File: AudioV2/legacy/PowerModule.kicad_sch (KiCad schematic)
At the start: 14 parts, among them J201 +15/-15/A_GND out, J202 PD module in (1=GND 2=+12V), U201 REC10K-2415DAW/H2, U202 L7809CV +9V

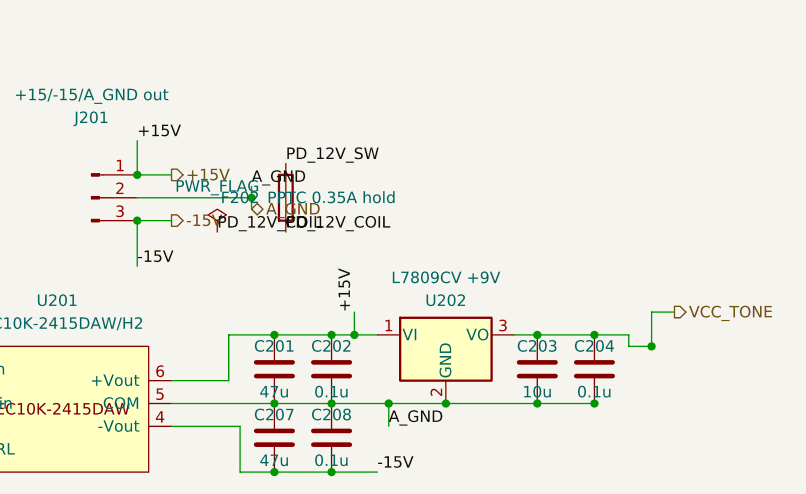
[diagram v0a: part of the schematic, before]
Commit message: AudioV2: D-f を実装した（+9V LDO 手前の PPTC 0.1A）。ゲート1は穴径だけ決めた
D-f —— 最後まで残っていた「各コンバータ手前に1本」の枝。

素材 legacy/PowerModule.kicad_sch を編集して再生成。+15V の T 点から U202.1 への
配線は 2.54 mm のスタブで 7.62 mm の素子が入らないため、D-g（F1603）と同じく
走行線から立ち上げて上で迂回し、F203 を縦置きにした。下流が無名ネットになり
power_pin_not_driven が出るので PWR_FLAG を1つ足してある。

  +15V(144.78,77.47) up (144.78,66.04) -> (147.32,66.04) down F203 down U202.VI(147.32,77.47)

⚠ これは保護の欠落を埋めたのではなく、方針の対称性。否定側査読の指摘どおり技術的
必須ではない（上流に主系ヒューズ、枝は ~30 mA、L7809 の熱保護もある）。残す判断の
理由は「1枝だけ幾何の都合で例外」を文書に抱え続けるコストの方が高いこと。定格
0.1 A はゲート3（U1604 の負荷電流実測）で再判定する。直列抵抗の落ちは 30 mA で
0.06〜0.15 V、±12 V 化時のヘッドルーム 3.0 V に対し 2〜5%。

ゲート1 —— 決めたのは穴径であって型番ではない。PCB は REC20K の穴径・ピン配置で
起こす。Ø1.0 → Ø1.4 の穴で起こせば REC10K は後からドロップインで戻せる（逆は不可）。
型番はゲート3とセットで決める: REC20K の代償である絶縁容量 1000 → 2000 pF の不利は
U1604 による既存のグランド結合への上乗せなので、U1604 を三端子へ替えるかで大きさが
変わるため。回路図の Value は REC10K-2415DAW/H2 のまま。

⚠ 1.2 kHz スパーでは絶縁容量の是非を判定できない（1000pF=133kΩ / 2000pF=66kΩ）。
効くのはスイッチング帯以上で、出方は ADC の床の持ち上がり。測る道具が別。

腐っていたドキュメントを4件直した:
  PARTS.md                     「PPTC は回路図には未追加」（3本すでにあった）
  AGENT_HANDOFF                「D-f/D-g PPTC 未実装2件」（D-g は 2026-09-04 に実装済み）
  DECISIONS 実装表 / +9V 共有表   D-f の「未実装」

検証（Windows / Git Bash / KiCad 10.0.6 / Docker 無し）:
  erc            29 件（内訳も従前と完全一致）
  netlist        部品 374 / 重複 0 / 注釈警告なし（373->374 は F203。PWR_FLAG は仮想で計上外）
  +15V           F203.1 を含み U202.1 は外れた
  新ネット        Net-(U202-VI) = [F203.2, U202.1]
  roundtrip      10 ファイル OK
  check_sexpr    問題 0
  再生成の冪等性   2回回して追加差分なし

Co-Authored-By: Claude Opus 5 <noreply@anthropic.com>
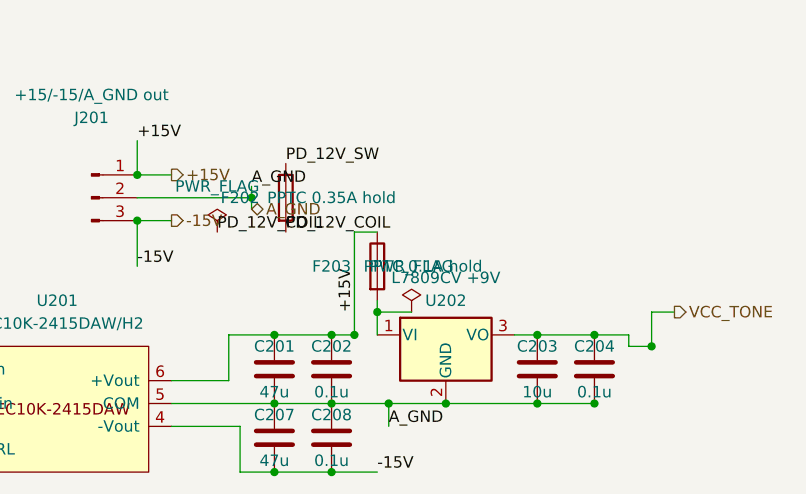
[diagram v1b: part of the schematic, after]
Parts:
- added F203: PPTC 0.1A hold, symbol Device:Fuse
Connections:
- net +15V: now also F203.1; no longer U202.1 (VI)
- new net: F203.2, U202.1 (VI)
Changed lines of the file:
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@@
-	(wire
-		(pts
-			(xy 144.78 77.47) (xy 147.32 77.47)
-		)
-		(stroke
-			(width 0)
-			(type default)
-		)
-	)
 	(wire
 		(pts
@@
 	(wire
 		(pts
-			(xy 144.78 74.93) (xy 144.78 77.47)
+			(xy 144.78 66.04) (xy 144.78 77.47)
 		)
 		(stroke
@@
 		)
 	)
+	(wire
+		(pts
+			(xy 144.78 66.04) (xy 147.32 66.04)
+		)
+		(stroke
+			(width 0)
+			(type default)
+		)
+	)
+	(wire
+		(pts
+			(xy 147.32 73.66) (xy 147.32 74.93)
+		)
+		(stroke
+			(width 0)
+			(type default)
+		)
+	)
+	(wire
+		(pts
+			(xy 147.32 74.93) (xy 147.32 77.47)
+		)
+		(stroke
+			(width 0)
+			(type default)
+		)
+	)
+	(wire
+		(pts
+			(xy 147.32 74.93) (xy 151.13 74.93)
+		)
+		(stroke
+			(width 0)
+			(type default)
+		)
+	)
+	(junction
+		(at 147.32 74.93)
+		(diameter 0)
+		(color 0 0 0 0)
+	)
+	(symbol
+		(lib_id "Device:Fuse")
+		(at 147.32 69.85 0)
+		(unit 1)
+		(body_style 1)
+		(exclude_from_sim no)
+		(in_bom yes)
+		(on_board yes)
+		(in_pos_files yes)
+		(dnp no)
+		(property "Reference" "F203"
+			(at 142.24 69.85 0)
+			(show_name no)
+			(do_not_autoplace no)
+			(effects
+				(font
+					(size 1.27 1.27)
+				)
+			)
+		)
+		(property "Value" "PPTC 0.1A hold"
+			(at 152.4 69.85 0)
+			(show_name no)
+			(do_not_autoplace no)
+			(effects
+				(font
+					(size 1.27 1.27)
+				)
+			)
+		)
+		(property "Footprint" ""
+			(at -12.7 45.72 0)
+			(hide yes)
+			(show_name no)
+			(do_not_autoplace no)
+			(effects
+				(font
+					(size 1.27 1.27)
+				)
+			)
+		)
+		(property "Datasheet" ""
+			(at -12.7 45.72 0)
+			(hide yes)
+			(show_name no)
+			(do_not_autoplace no)
+			(effects
+				(font
+					(size 1.27 1.27)
+				)
+			)
+		)
+		(property "Description" ""
+			(at -12.7 45.72 0)
+			(hide yes)
+			(show_name no)
+			(do_not_autoplace no)
+			(effects
+				(font
+					(size 1.27 1.27)
+				)
+			)
+		)
+		(pin "1"
+		)
+		(pin "2"
+		)
+		(instances
+			(project "AudioV2Case"
+				(path "/a1000001-0001-4001-8001-000000000001/a1000002-0002-4002-8002-000000000002"
+					(reference "F203")
+					(unit 1)
+				)
+			)
+		)
+	)
 	(label "PD_12V_SW"
 		(at 137.16 58.42 0)
@@
 					(unit 1)
 				)
+			)
+		)
+	)
+	(symbol
+		(lib_id "power:PWR_FLAG")
+		(at 151.13 74.93 0)
+		(unit 1)
+		(body_style 1)
+		(exclude_from_sim no)
+		(in_bom yes)
+		(on_board yes)
+		(in_pos_files yes)
+		(dnp no)
+		(fields_autoplaced yes)
+		(property "Reference" "#FLG0204"
+			(at 151.13 72.39 0)
+			(hide yes)
+			(show_name no)
+			(do_not_autoplace no)
+			(effects
+				(font
+					(size 1.27 1.27)
+				)
+			)
+		)
+		(property "Value" "PWR_FLAG"
+			(at 151.13 69.85 0)
+			(show_name no)
+			(do_not_autoplace no)
+			(effects
+				(font
+					(size 1.27 1.27)
+				)
+			)
+		)
+		(property "Footprint" ""
+			(at 74.93 88.9 0)
+			(hide yes)
+			(show_name no)
+			(do_not_autoplace no)
+			(effects
+				(font
+					(size 1.27 1.27)
+				)
+			)
+		)
+		(property "Datasheet" ""
+			(at 74.93 88.9 0)
+			(hide yes)
+			(show_name no)
+			(do_not_autoplace no)
+			(effects
+				(font
+					(size 1.27 1.27)
+				)
+			)
+		)
+		(property "Description" "Special symbol for telling ERC where power comes from"
+			(at 74.93 88.9 0)
+			(hide yes)
+			(show_name no)
+			(do_not_autoplace no)
+			(effects
+				(font
+					(size 1.27 1.27)
+				)
+			)
+		)
+		(pin "1"
+		)
+		(instances
+			(project "AudioV2Case"
+				(path "/a1000001-0001-4001-8001-000000000001/a1000002-0002-4002-8002-000000000002"
+					(reference "#FLG0204")
+					(unit 1)
+				)

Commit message: AudioV2: 母板のフットプリント 23 個を設計内の前例に合わせて埋めた（39 -> 16）
B5 の下ごしらえ。前例のあるものだけを埋め、判断が要るものには触っていない。

  積セラ 1206     C202/204/206/208/402, C403/404/410/411, C408/412
                  設計で 85 回使われている流儀に合わせた
  抵抗 1206       R410/411（同 128 回）
  フィルム        C405/406/407/409（2.2u）
                  PT2314 の入出力結合で音声が通る。設計内の C601「2.2uF film」と
                  同じ footprint に揃えた。セラミックは電圧で容量が変わるので
                  結合位置に置くと歪む（ユーザー判断 2026-09-07）
  電解            C201/205/207(47u) -> D8.0/P3.50（C1610・C1621 と同じ）
                  C401(22u)         -> D6.3/P2.50（C1630 と同じ）
                  C203(10u)         -> D5.0/P2.00（C1635「10uF 50V」と同じ）
  DC-DC           U403 -> Library:BP5293-50_ROHM_SIP-3
                  U1607 が同一部品で同じ footprint

素材（legacy/ControlPanelAnalog 15個・legacy/PowerModule 8個）を編集して再生成した。

**残り 16 個には触っていない。** 性質が2つに分かれる:

  パネル部品 6（RV501/502・SW501/502/1601・SW402）
    KiCad にもプロジェクトの Audio/Library.pretty にも footprint が無い。
    Alps は RK097/RK09K しかなく RK27 は別物。C&K 7000 系トグルも無い。
    データシートから新規に作る作業になる。
    さらに SW501/502/1601 は現物1個の 3PDT を3シンボルで表しているので、
    3つ全部に footprint を入れると PCB にスイッチが3個並ぶ。1個化が要る。

  調達判断待ち 10（D403・F201/202/203・J201/202・J_HP501・J_LINE501・
    J_RAIL501・U202）

検証:
  未設定      39 -> 16
  netlist     部品 370 / 重複 0（変化なし）
  erc         17 件（変化なし）
  check_sexpr 13 ファイル / 問題 0
  roundtrip   6/6 OK
  再生成      2回目でバイト一致

Co-Authored-By: Claude Opus 5 <noreply@anthropic.com>
Claude-Session: https://claude.ai/code/session_01VCArLcCGbMGgxvWJ5HFJiY
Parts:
- C201, C205, C207: footprint (none) -> Capacitor_THT:CP_Radial_D8.0mm_P3.50mm
- C202, C204, C206, C208: footprint (none) -> Capacitor_SMD:C_1206_3216Metric_Pad1.33x1.80mm_HandSolder
- C203: footprint (none) -> Capacitor_THT:CP_Radial_D5.0mm_P2.00mm
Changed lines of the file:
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@@
 			)
 		)
-		(property "Footprint" ""
+		(property "Footprint" "Capacitor_THT:CP_Radial_D5.0mm_P2.00mm"
 			(at 22.86 10.16 0)
 			(hide yes)
@@
 			)
 		)
-		(property "Footprint" ""
+		(property "Footprint" "Capacitor_THT:CP_Radial_D8.0mm_P3.50mm"
 			(at -1.27 20.32 0)
 			(hide yes)
@@
 			)
 		)
-		(property "Footprint" ""
+		(property "Footprint" "Capacitor_SMD:C_1206_3216Metric_Pad1.33x1.80mm_HandSolder"
 			(at -62.23 21.59 0)
 			(hide yes)
@@
 			)
 		)
-		(property "Footprint" ""
+		(property "Footprint" "Capacitor_SMD:C_1206_3216Metric_Pad1.33x1.80mm_HandSolder"
 			(at 3.81 10.16 0)
 			(hide yes)
@@
 			)
 		)
-		(property "Footprint" ""
+		(property "Footprint" "Capacitor_SMD:C_1206_3216Metric_Pad1.33x1.80mm_HandSolder"
 			(at -7.62 17.78 0)
 			(hide yes)
@@
 			)
 		)
-		(property "Footprint" ""
+		(property "Footprint" "Capacitor_SMD:C_1206_3216Metric_Pad1.33x1.80mm_HandSolder"
 			(at -7.62 25.4 0)
 			(hide yes)
@@
 			)
 		)
-		(property "Footprint" ""
+		(property "Footprint" "Capacitor_THT:CP_Radial_D8.0mm_P3.50mm"
 			(at -1.27 17.78 0)
 			(hide yes)
@@
 			)
 		)
-		(property "Footprint" ""
+		(property "Footprint" "Capacitor_THT:CP_Radial_D8.0mm_P3.50mm"
 			(at -8.89 31.75 0)
 			(hide yes)

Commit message: AudioV2: 端子台5個を Phoenix MKDS-1,5 にした（10 -> 5）
ユーザー判断（2026-09-07）。PARTS.md:211 が板間の端子台に Phoenix MKDS-1,5
系を指定しており、計測基板の J1601(2P) / J1603(3P) に既に同じ footprint が
入っている。その前例に合わせた。

  J201       1x03  +15/-15/A_GND out
  J202       1x02  PD module in
  J_HP501    1x02  to Audio HP Buffer
  J_LINE501  1x02  LINE OUT
  J_RAIL501  1x03  RAIL IN

J_HP501 / J_LINE501 / J_RAIL501 は元から Connector:Screw_Terminal_01xNN
シンボルなので端子台が自然。J201 / J202 は Conn_01xNN_Pin（汎用ピン）だが、
板間の電源なので同じ系に揃えた。

残り5個は性質が違うので手を付けていない:
  D403             12V パネル LED。直列抵抗の有無が未決（DECISIONS の既知項目）
  F201             T1.6A slow 5x20。ヒューズホルダの品種
  F202/F203        PPTC。MPN 未確定（直流抵抗とディレーティングが決まらない）
  U202             L7809CV TO-220。実装向き（垂直/水平・放熱器）が機構判断

検証:
  未設定      10 -> 5
  netlist     部品 370 / 重複 0（変化なし）
  erc         17 件（変化なし）
  check_sexpr 13 ファイル / 問題 0
  roundtrip   6/6 OK
  再生成      2回目でバイト一致

Co-Authored-By: Claude Opus 5 <noreply@anthropic.com>
Claude-Session: https://claude.ai/code/session_01VCArLcCGbMGgxvWJ5HFJiY
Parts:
- J201: footprint (none) -> TerminalBlock_Phoenix:TerminalBlock_Phoenix_MKDS-1,5-3-5.08_1x03_P5.08mm_Horizontal
- J202: footprint (none) -> TerminalBlock_Phoenix:TerminalBlock_Phoenix_MKDS-1,5-2-5.08_1x02_P5.08mm_Horizontal
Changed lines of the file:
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@@
 			)
 		)
-		(property "Footprint" ""
+		(property "Footprint" "TerminalBlock_Phoenix:TerminalBlock_Phoenix_MKDS-1,5-2-5.08_1x02_P5.08mm_Horizontal"
 			(at 26.67 -5.08 0)
 			(hide yes)
@@
 			)
 		)
-		(property "Footprint" ""
+		(property "Footprint" "TerminalBlock_Phoenix:TerminalBlock_Phoenix_MKDS-1,5-3-5.08_1x03_P5.08mm_Horizontal"
 			(at -59.69 6.35 0)
 			(hide yes)

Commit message: AudioV2: 残り5個のフットプリントを埋めた（5 -> 0）。D403 に直列抵抗 R401
フットプリント未設定 0 個。これで netlist 上の 371 部品すべてに footprint が付いた。

- F201/F202/F203 … Resistor_THT:R_Axial_DIN0411_L9.9mm_D3.6mm_P12.70mm_Horizontal
  設計内の F1601/F1602/F1603 と同じリード品に揃えた。ピッチが3種類に散らばる
  より、入手性のいい 5x20mm 相当の軸形1種に寄せたほうが調達が楽になる
- U202 … Package_TO_SOT_THT:TO-220-3_Vertical
  垂直立て。放熱器の要否と向きは PCB を起こすとき（B5）に決め直す
- D403 … LED_THT:LED_D5.0mm（設計内の D1610/D1611 と同じ）

D403 は PD_12V_SW に直付けだったので、電流制限の 2.2k を直列に入れた:

    PD_12V_SW ─[R401 2.2k]─ LED_12V_A ─[D403]─ PD_GND

抵抗なしだと LED の Vf ばらつきがそのまま電流に出る。12V で Vf 2.0V 想定なら
約 4.5mA。部品数 370 -> 371（CLAUDE.md の期待値も更新）。

生成シートは直接触らず、素材の legacy/ControlPanelAnalog.kicad_sch と
legacy/PowerModule.kicad_sch を編集して build_daughter -> build_motherboard で
再生成した。

検証:
  check_sexpr.py -q AudioV2        13 ファイル / 問題 0
  kicad-run.sh erc                 17 件（変化なし）
  kicad-run.sh netlist             部品 371 個・重複 0・footprint 未設定 0
  sch_import.py --roundtrip        6/6 OK
  再生成の冪等性                    バイト一致

⚠ PARTS.md の「音声 2×4」は「4ピンのヘッダを2組」と読んで 2 x PinHeader_1x04 に
した。2行4列（PinHeader_2x04）のつもりだったなら直す必要がある。

Co-Authored-By: Claude Opus 5 <noreply@anthropic.com>
Claude-Session: https://claude.ai/code/session_01VCArLcCGbMGgxvWJ5HFJiY
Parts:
- F201, F202, F203: footprint (none) -> Resistor_THT:R_Axial_DIN0411_L9.9mm_D3.6mm_P12.70mm_Horizontal
- U202: footprint (none) -> Package_TO_SOT_THT:TO-220-3_Vertical
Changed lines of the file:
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@@
 			)
 		)
-		(property "Footprint" ""
+		(property "Footprint" "Package_TO_SOT_THT:TO-220-3_Vertical"
 			(at 0 11.43 0)
 			(hide yes)
@@
 			)
 		)
-		(property "Footprint" ""
+		(property "Footprint" "Resistor_THT:R_Axial_DIN0411_L9.9mm_D3.6mm_P12.70mm_Horizontal"
 			(at -12.7 45.72 0)
 			(hide yes)
@@
 			)
 		)
-		(property "Footprint" ""
+		(property "Footprint" "Resistor_THT:R_Axial_DIN0411_L9.9mm_D3.6mm_P12.70mm_Horizontal"
 			(at -12.7 45.72 0)
 			(hide yes)
@@
 			)
 		)
-		(property "Footprint" ""
+		(property "Footprint" "Resistor_THT:R_Axial_DIN0411_L9.9mm_D3.6mm_P12.70mm_Horizontal"
 			(at -12.7 45.72 0)
 			(hide yes)

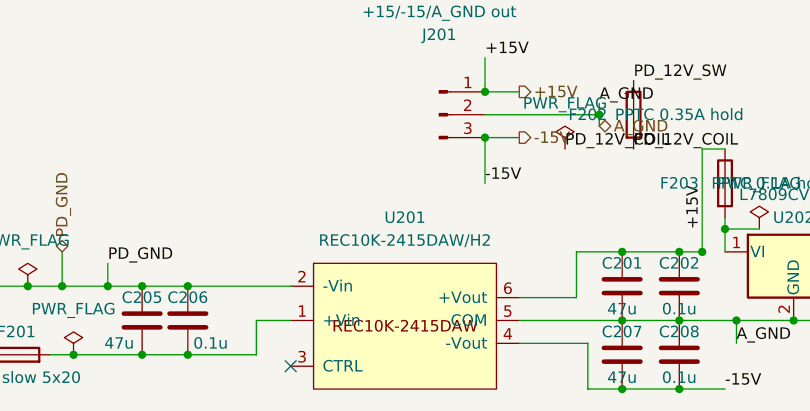
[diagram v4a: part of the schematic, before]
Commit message: AudioV2: DC-DC を REC20K-2415DZ へ差し替え、電源要求を「ソケットあたり」で記録した
## なぜ

この箱はオペアンプを差し替えて聴く箱で、入力ブロードキャスト＋出力のみ MUX なので
10個が常時通電する。つまり +15V の要求は「NE5532 ×10」ではなく「挿す石 ×10、常時」で、
レールの余裕は**1ソケットあたり何 mA 使えるか**に翻訳しないと目的と噛み合わない。

Audio/datasheets/opamps/ の一次資料（在庫石の Icc）:
  MUSES03  20 mA/socket（10 mA max ×2 の変換基板）← 在庫の最悪
  NE5532   16 mA（ICC total、VO=0 無負荷。typ 6 mA）
  OPA627×2 15 mA / LT1364 15 mA / OPA1656 9.2 mA/pkg max

1ソケットあたりに使える電流（固定側を保守側の 63 mA として）:

              計測系そのまま  LDO を +15V へ  +5V_D も +15V へ
  REC10K       27.0 mA        19.0 mA         9.4 mA
  REC20K       60.4 mA        52.4 mA        42.8 mA

REC10K では計測系を触らなくても 27 mA/socket しか出ない。MUSES03(20mA) は通るが
ディスクリート DIP-8 モジュールは入らず、計測系を +15V へ寄せると NE5532 の max
16 mA すら割る。「差し替えて遊ぶ」という目的に対して REC10K は最初から窮屈だった。

## 差し替え

独立した3つの理由が同じ結論に集まった:
  ① 上のソケットあたり予算
  ② Cout の宿題 — 実レール容量は +15V/-15V とも 259.8uF（sch_facts rails）で
     REC10K の Cout ±270uF の 96%。記録が使ってきた「102uF」は娘基板のバルクが
     入る前の古い値だった。REC20K は ±3000uF で 11 倍の余裕
  ③ 計測系の電源を +15V へ寄せる余地（U1604 = 非絶縁バック = 1.2kHz スパーの
     容疑者を設計から消せる。これ自体は未実施）

DS を突き合わせた結果（Recom_REC20K-Z_Rev3-2025.pdf p9 / REC10K-AW_Rev2-2025.pdf p9）:
入力 9-36V・ピン配置・パッド座標は同一で、**違うのは推奨穴だけ**（Ø1.0 -> Ø1.4）。

  ⚠ NOW.md は以前から「PCB の穴径は REC20K 互換（Ø1.4）」と書いていたが、
    フットプリント REC10K-AW_1in_THT は drill 1.0 のままで意図が実装されていなかった。
    REC20K の 1.4mm ピンは入らない。

Library:REC20K-Z_1in_THT を新設（穴 Ø1.4・パッド 2.2mm で環状部 0.4mm 維持）。
Ø1.4 なら REC10K（ピン径 0.6）も挿さるので、この1個で両方いける
= NOW.md の「REC10K は後から戻せる」が本当に成立する形になった。

  AudioV2.kicad_sym            REC20K-2415DZ を追加（REC10K とピン配置同一）
  legacy/PowerModule.kicad_sch U201 の lib_id/Value/Footprint/Datasheet/Description
                               ⚠ .kicad_sch は先頭に lib_symbols のキャッシュを持つので
                                 キャッシュと実体の2箇所を直す必要がある

## F201（入口 T1.6A）は据え置いたが、意味が変わった

12V 入力・効率 88% で:
  いまの想定（10×20mA + 固定 63mA）  7.9 W → 0.75 A  (T1.6A の 47%)
  計測系を +15V へ寄せたとき        10.5 W → 1.00 A  (62%)
  REC20K を使い切ったとき           20.0 W → 1.89 A  (118%)

つまり F201 が「REC20K の能力ではなく設計予算」を上限にしている。意図的なら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
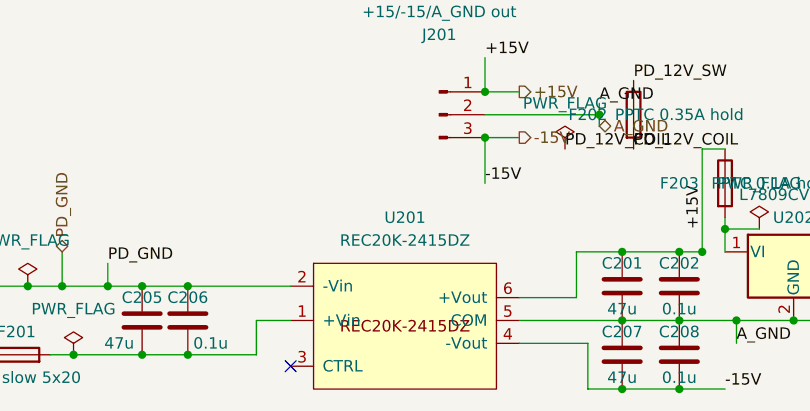
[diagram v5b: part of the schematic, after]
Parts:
- U201: value REC10K-2415DAW/H2 -> REC20K-2415DZ; footprint Library:REC10K-AW_1in_THT -> Library:REC20K-Z_1in_THT; symbol AudioV2:REC10K-2415DAW -> AudioV2:REC20K-2415DZ; MPN REC10K-2415DAW/H2 -> REC20K-2415DZ
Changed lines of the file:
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@@
 	)
 	(symbol
-		(lib_id "AudioV2:REC10K-2415DAW")
+		(lib_id "AudioV2:REC20K-2415DZ")
 		(at 111.76 76.2 0)
 		(unit 1)
@@
 			)
 		)
-		(property "Value" "REC10K-2415DAW/H2"
+		(property "Value" "REC20K-2415DZ"
 			(at 111.76 76.2 0)
 			(show_name no)
@@
 			)
 		)
-		(property "Footprint" "Library:REC10K-AW_1in_THT"
+		(property "Footprint" "Library:REC20K-Z_1in_THT"
 			(at 113.03 72.39 0)
 			(hide yes)
@@
 			)
 		)
-		(property "Datasheet" "https://recom-power.com/pdf/Econoline/REC10K-AW.pdf"
+		(property "Datasheet" "AudioV2/datasheets/Recom_REC20K-Z_Rev3-2025.pdf"
 			(at 112.268 74.422 0)
 			(hide yes)
@@
 			)
 		)
-		(property "Description" "Recom REC10K-2415DAW/H2 isolated DC/DC, 9-36Vin, ±15V/±333mA (10W), 1.6kVDC iso, DIP 1in x 1in, Cout ±270uF/rail, pin3=CTRL open=ON"
+		(property "Description" "Recom REC20K-2415DZ isolated DC/DC, 9-36Vin, ±15V/±667mA (20W), eff 88% typ, DIP 1in x 1in, Cout ±3000uF/rail, pin3=CTRL open=ON。REC10K-2415DAW/H2（±333mA・Cout ±270uF）から 2026-09-07 に差し替えた。理由は独立に3つ: ①ソケット10個が常時通電なので ±333mA だと 1ソケットあたり 27mA しか使えず、在庫の MUSES03（20mA）で既に窮屈 ②実レール容量 259.8uF が Cout ±270uF の 96% ③計測系の電源を +15V へ寄せる余地。ピン配置は REC10K と同一で、推奨穴が Ø1.0 -> Ø1.4 になるのでフットプリントも替えた（Ø1.4 なら REC10K も挿さる）"
 			(at 111.76 76.2 0)
 			(hide yes)
@@
 			)
 		)
-		(property "MPN" "REC10K-2415DAW/H2"
+		(property "MPN" "REC20K-2415DZ"
 			(at 111.76 76.2 0)
 			(hide yes)

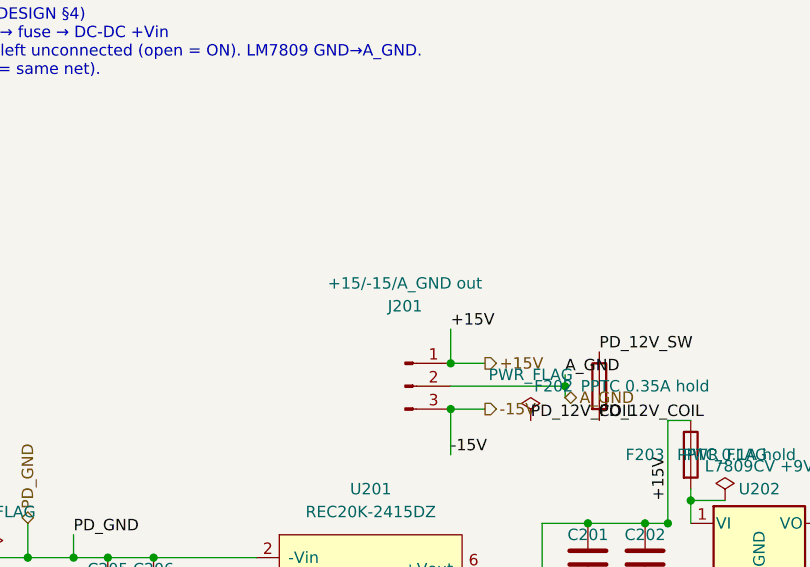
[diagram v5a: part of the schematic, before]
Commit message: AudioV2: J1602 / J1603 のピン並びを母板の J202 / J201 に揃えた
計測側の電源端子が母板側と逆順だった（J1603: -15/GND/+15 vs J201: +15/A_GND/-15、
J1602: +12V/GND vs J202: GND/+12V）。配線・ラベル・F1601 は動かさず、シンボルを
左右ミラーしてピンの x を入れ替えた（J1602 はアンカーも 1 ピッチ移動）。
J201 の Value「+15/-15/A_GND out」を実ピン順「+15/A_GND/-15 out」に直した（素材 → 再生成）。
端子を残すか外すかは B5 のハーネス判断のまま。J1601（AUDIO、R/L 2P）は J_RAIL501（L/A_GND/R 3P）
と形が違う点を NOW に書いた。

検証: kicad-cli ネットリストで J1603 1=+15V 2=A_GND 3=-15V、J1602 1=PD_GND 2=F1601 側を確認。
ERC 11 件（変化なし）・部品 389・重複 0・check_sexpr 0・roundtrip OK・再生成バイト一致。

Co-Authored-By: Claude Fable 5.1 <noreply@anthropic.com>
Claude-Session: https://claude.ai/code/session_01VCArLcCGbMGgxvWJ5HFJiY
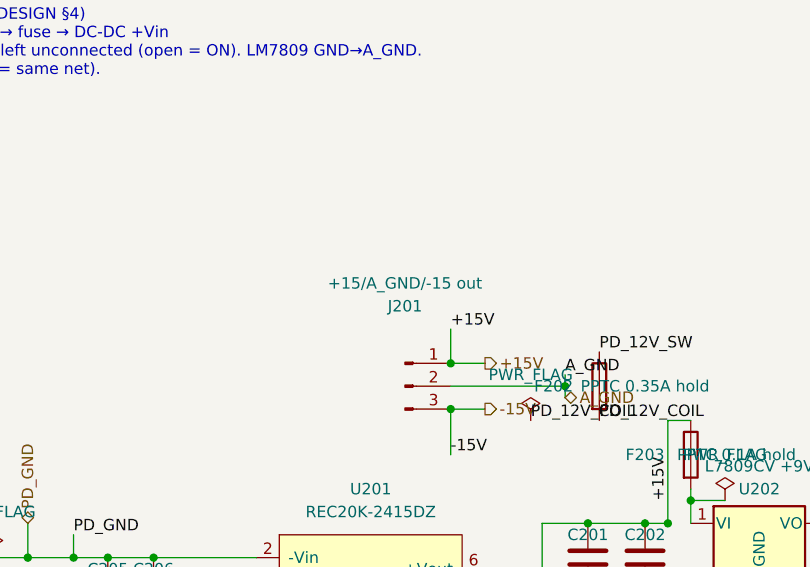
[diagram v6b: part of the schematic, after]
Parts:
- J201: value +15/-15/A_GND out -> +15/A_GND/-15 out
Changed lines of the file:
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@@
 			)
 		)
-		(property "Value" "+15/-15/A_GND out"
+		(property "Value" "+15/A_GND/-15 out"
 			(at 115.57 50.8 0)
 			(show_name no)
